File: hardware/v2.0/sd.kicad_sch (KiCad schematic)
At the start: 3 parts, among them J6 Micro_SD_Card_Det2, U1 ECP5U-25F-CABGA256

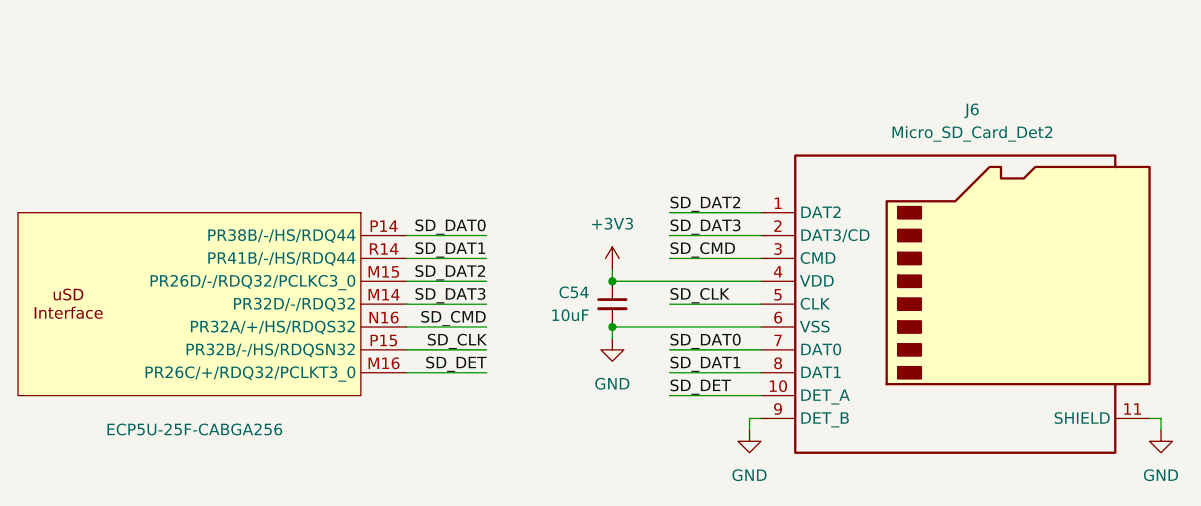
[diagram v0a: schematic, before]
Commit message: ADC 6 diff lines
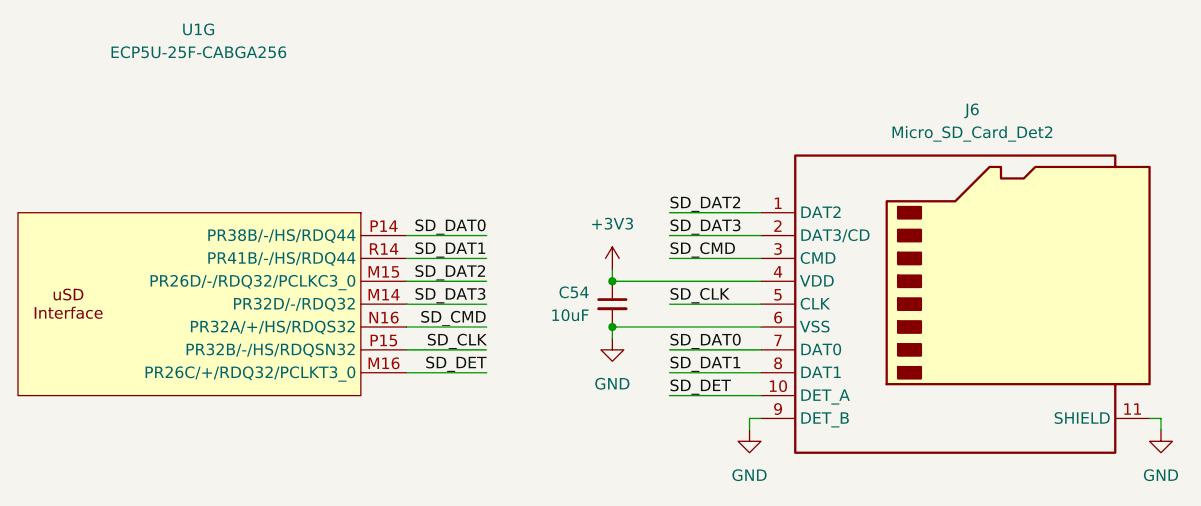
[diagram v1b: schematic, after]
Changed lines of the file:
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@@
 		(dnp no)
 		(property "Reference" "U1"
-			(at 102.108 29.972 0)
+			(at 101.346 67.31 0)
 			(effects
 				(font
 					(size 1.27 1.27)
 				)
-				(hide yes)
 			)
 		)
 		(property "Value" "ECP5U-25F-CABGA256"
-			(at 110.744 111.76 0)
+			(at 101.346 69.85 0)
 			(effects
 				(font
 					(size 1.27 1.27)
 				)
-				(justify left)
 			)
 		)
@@
 					(reference "U1")
 					(unit 7)
+				)
+				(path "/f88da08e-cf42-4d03-a08f-3f602fe6658d/b5a9aa02-311b-4a9a-a7d4-646f15cdd9c2"
+					(reference "U1")
+					(unit 7)

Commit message: ADC CLKOUT±
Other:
- company: Chengyin Yao (cheyao), Vadym Vikulin -> Vadym Vikulin, Chengyin Yao (cheyao)
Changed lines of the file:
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@@
 	(title_block
 		(title "Icepi Zero")
-		(date "2026-01-05")
-		(rev "v2.0")
-		(company "Chengyin Yao (cheyao), Vadym Vikulin")
-		(comment 1 "https://github.com/cheyao/icepi-zero")
+		(date "2026-01-17")
+		(rev "v2.1")
+		(company "Vadym Vikulin, Chengyin Yao (cheyao)")
+		(comment 1 "https://github.com/vikulin/icepi-zero")
 		(comment 2 "License: Solderpad")
+		(comment 9 "OSHWA FR000026")
 	)
 	(junction
@@
 		(pin "F8"
 		)
+		(pin "N6"
+		)
 		(instances

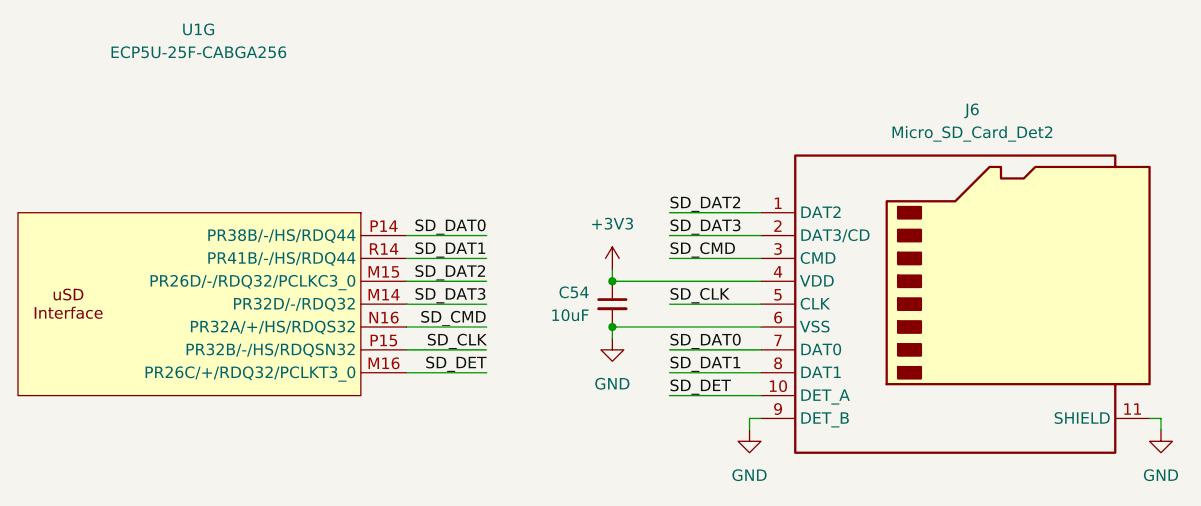
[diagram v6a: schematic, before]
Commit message: BOM fields unification for PCBWay requirements
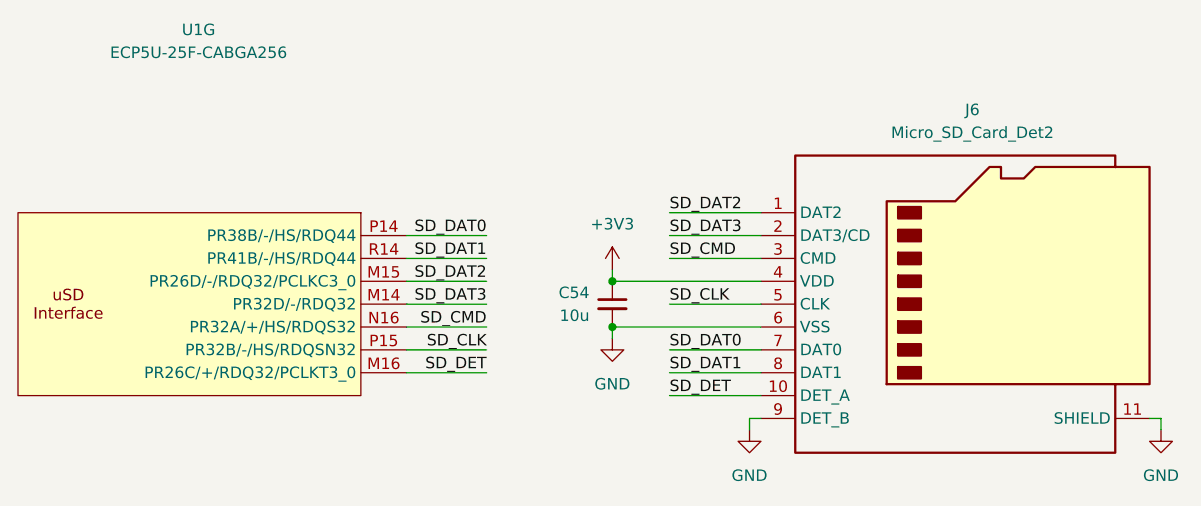
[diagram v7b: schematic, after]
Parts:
- C54: value 10uF -> 10u; MANUFACTURER (none) -> Samsung Electro-Mechanics; MANUFACTURER_PART_NUMBER (none) -> CL10A106KP8NNNC
- J6: MANUFACTURER (none) -> SOFNG; MANUFACTURER_PART_NUMBER (none) -> TF-008
- U1: MANUFACTURER (none) -> Lattice; MANUFACTURER_PART_NUMBER (none) -> LFE5U-25F-6BG256C
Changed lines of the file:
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@@
 			)
 		)
-		(property "Value" "10uF"
+		(property "Value" "10u"
 			(at 144.78 99.0662 0)
 			(effects
@@
 			)
 		)
-		(property "Description" "Unpolarized capacitor, small symbol"
+		(property "Description" "Unpolarized capacitor"
 			(at 147.32 97.79 0)
 			(effects
@@
 		)
 		(property "Notes" ""
+			(at 147.32 97.79 0)
+			(effects
+				(font
+					(size 1.27 1.27)
+				)
+				(hide yes)
+			)
+		)
+		(property "Original" ""
+			(at 147.32 97.79 0)
+			(effects
+				(font
+					(size 1.27 1.27)
+				)
+				(hide yes)
+			)
+		)
+		(property "Instructions/Notes" ""
+			(at 147.32 97.79 0)
+			(effects
+				(font
+					(size 1.27 1.27)
+				)
+				(hide yes)
+			)
+		)
+		(property "MANUFACTURER_PART_NUMBER" "CL10A106KP8NNNC"
+			(at 147.32 97.79 0)
+			(effects
+				(font
+					(size 1.27 1.27)
+				)
+				(hide yes)
+			)
+		)
+		(property "MANUFACTURER" "Samsung Electro-Mechanics"
 			(at 147.32 97.79 0)
 			(effects
@@
 			)
 		)
+		(property "Original" ""
+			(at 100.33 97.79 0)
+			(effects
+				(font
+					(size 1.27 1.27)
+				)
+				(hide yes)
+			)
+		)
+		(property "Instructions/Notes" ""
+			(at 100.33 97.79 0)
+			(effects
+				(font
+					(size 1.27 1.27)
+				)
+				(hide yes)
+			)
+		)
+		(property "MANUFACTURER" "Lattice"
+			(at 100.33 97.79 0)
+			(effects
+				(font
+					(size 1.27 1.27)
+				)
+				(hide yes)
+			)
+		)
+		(property "MANUFACTURER_PART_NUMBER" "LFE5U-25F-6BG256C"
+			(at 100.33 97.79 0)
+			(effects
+				(font
+					(size 1.27 1.27)
+				)
+				(hide yes)
+			)
+		)
 		(pin "T2"
 		)
@@
 			(at 186.69 97.79 0)
 			(effects
+				(font
+					(size 1.27 1.27)
+				)
+				(hide yes)
+			)
+		)
+		(property "Original" ""
+			(at 186.69 97.79 0)
+			(effects
+				(font
+					(size 1.27 1.27)
+				)
+				(hide yes)
+			)
+		)
+		(property "Instructions/Notes" ""
+			(at 186.69 97.79 0)
+			(effects
+				(font
+					(size 1.27 1.27)
+				)
+				(hide yes)
+			)
+		)
+		(property "MANUFACTURER" "SOFNG"
+			(at 186.69 97.79 0)
+			(effects
+				(font
+					(size 1.27 1.27)
+				)
+				(hide yes)
+			)
+		)
+		(property "MANUFACTURER_PART_NUMBER" "TF-008"
+			(at 186.69 97.79 0)
+			(effects
